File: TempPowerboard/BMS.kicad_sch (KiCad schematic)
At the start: 77 parts, among them IC1 BQ7694204PFBR, J1 Batt_Cells, J2 PEC02SAAN, Q1 NMOS, Q2 NMOS, Q3 NMOS, Q4 NMOS, Q5 FCX495TA

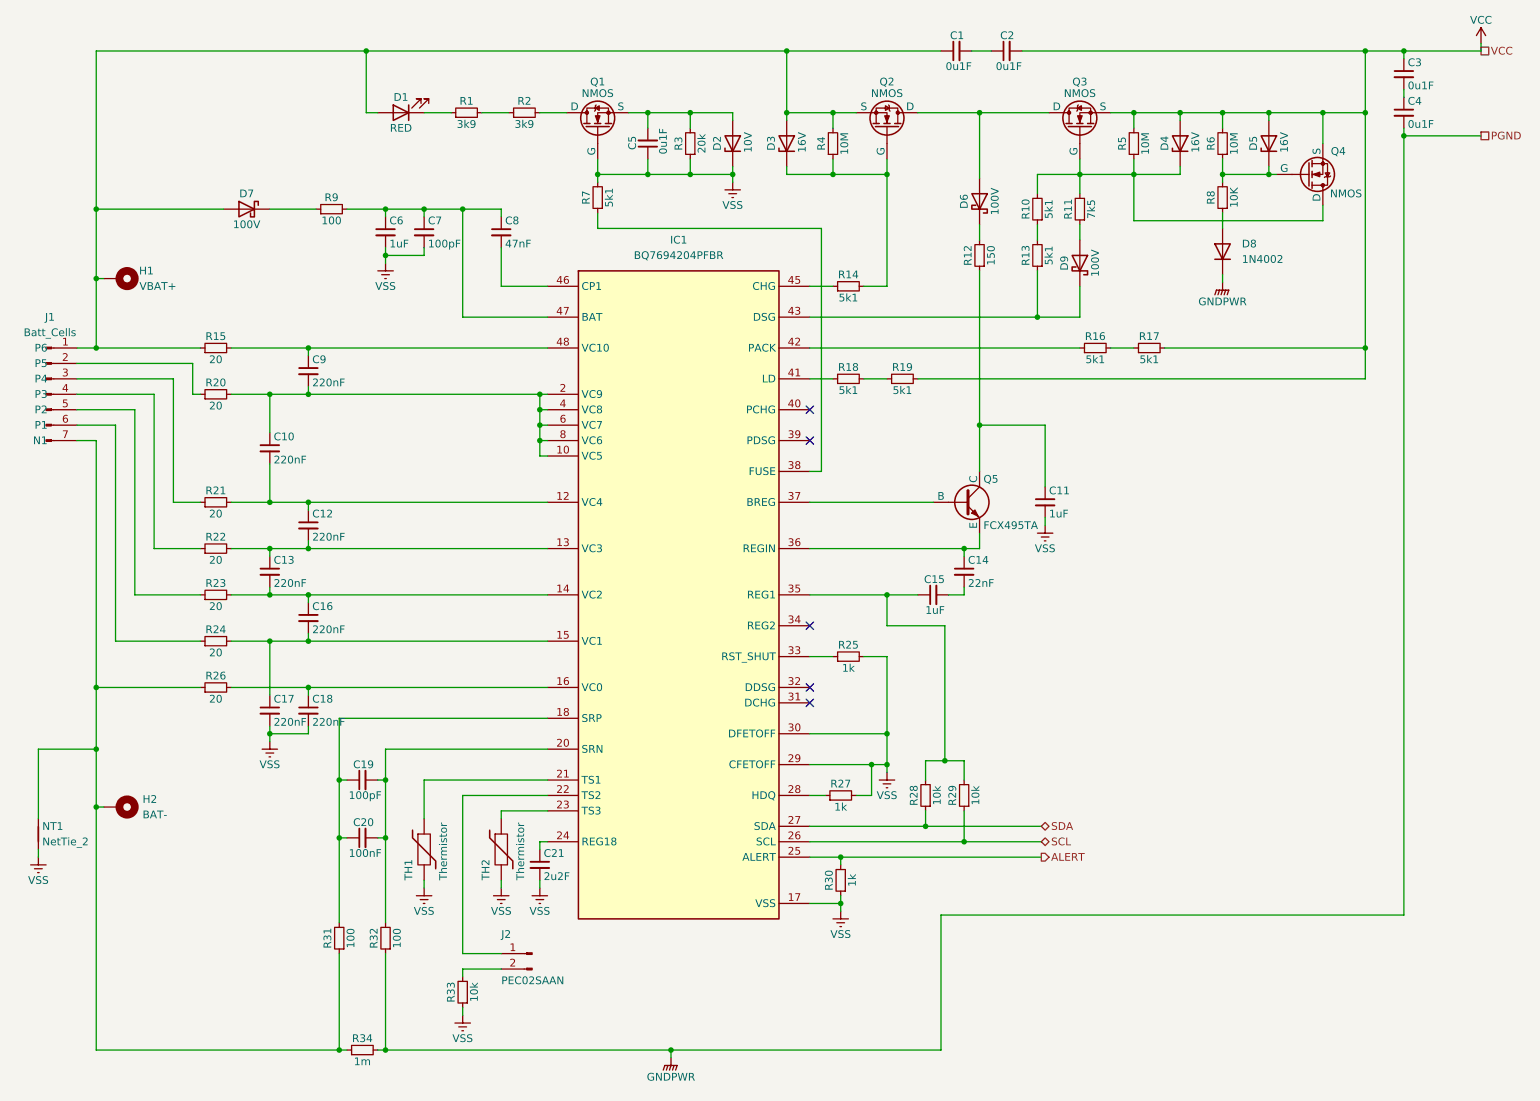
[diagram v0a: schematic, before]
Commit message: Devboard ports defined
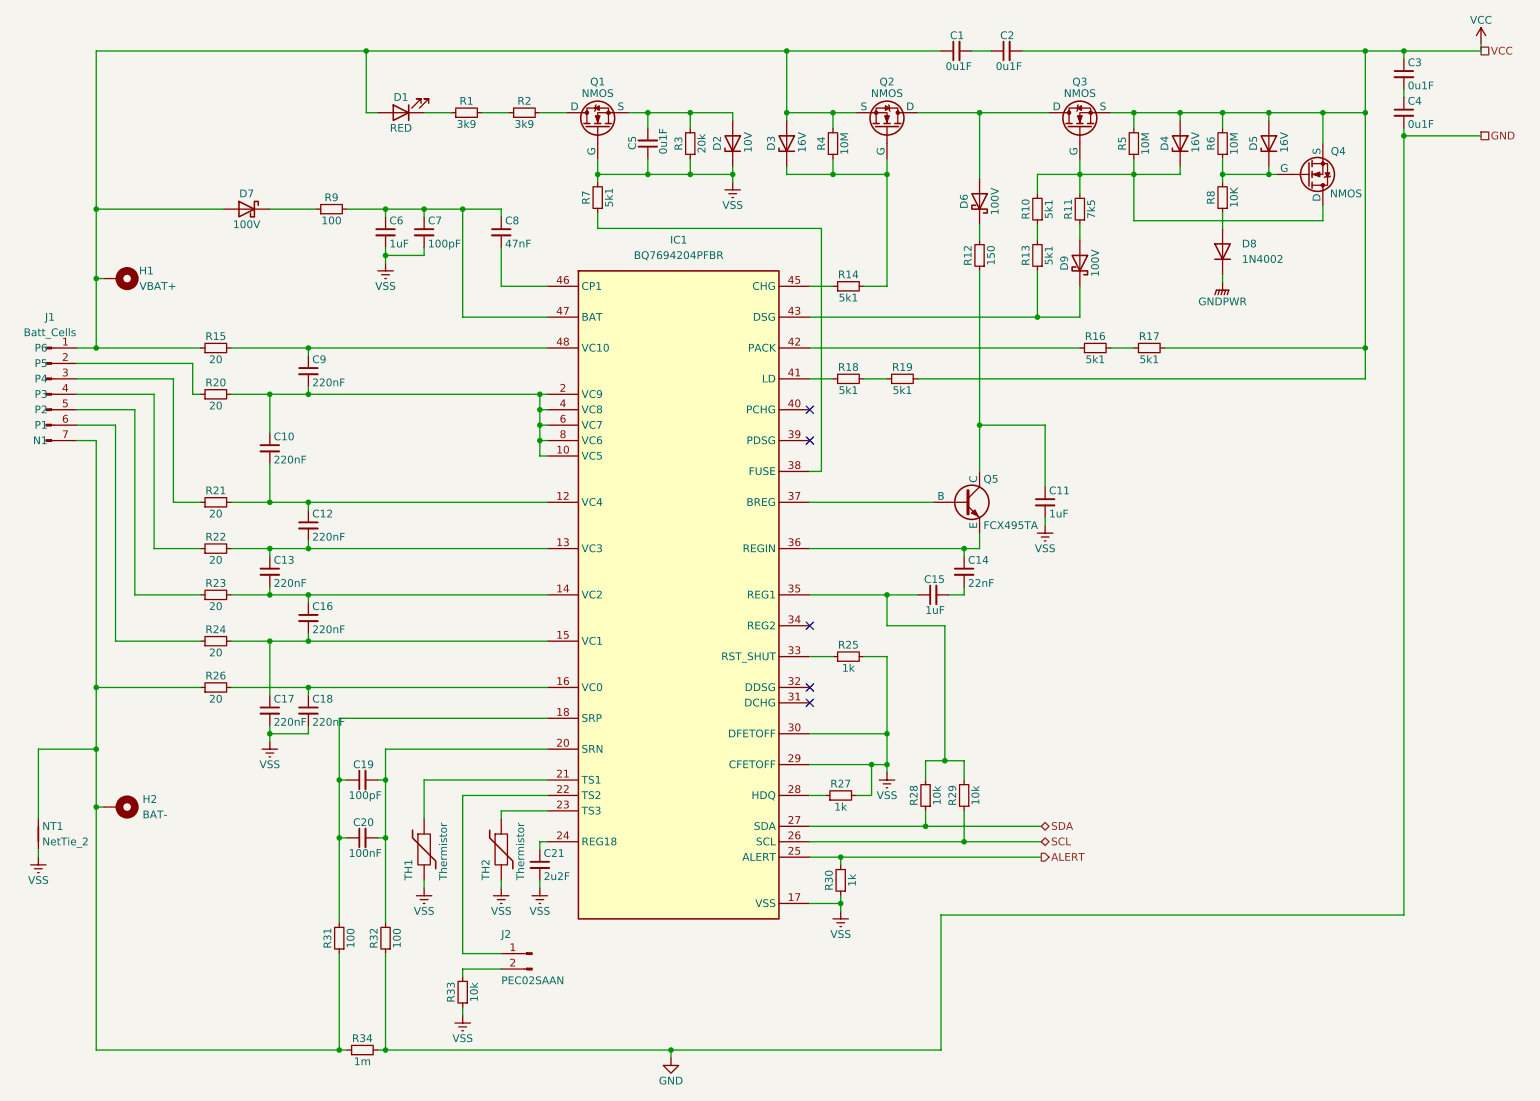
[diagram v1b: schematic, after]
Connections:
- net GNDPWR: no longer C4.2, R32.1, R34.2
- new net GND: C4.2, R32.1, R34.2
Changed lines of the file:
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@@
     (effects (font (size 1.27 1.27)) (justify left))
   )
-  (hierarchical_label "PGND" (shape passive) (at 260.35 33.655 0) (fields_autoplaced)
+  (hierarchical_label "GND" (shape passive) (at 260.35 33.655 0) (fields_autoplaced)
     (effects (font (size 1.27 1.27)) (justify left))
   )
@@
     )
   )
+  (symbol (lib_id "power:GND") (at 127 185.42 0) (unit 1)
+    (in_bom yes) (on_board yes) (dnp no)
+    (property "Reference" "#PWR023" (at 127 191.77 0)
+      (effects (font (size 1.27 1.27)) hide)
+    )
+    (property "Value" "GND" (at 127 189.23 0)
+      (effects (font (size 1.27 1.27)))
+    )
+    (property "Footprint" "" (at 127 185.42 0)
+      (effects (font (size 1.27 1.27)) hide)
+    )
+    (property "Datasheet" "" (at 127 185.42 0)
+      (effects (font (size 1.27 1.27)) hide)
+    )
+    (pin "1")
+    (instances
+      (project "TempPowerboard"
+        (path "/99c105bb-32a2-4c72-8069-227e584b9994/1eab3a2e-b7d4-4587-9e17-7f816eae63ec"
+          (reference "#PWR023") (unit 1)
+        )
+      )
+    )
+  )
   (symbol (lib_id "power:Earth") (at 137.16 41.275 0) (unit 1)
     (in_bom yes) (on_board yes) (dnp no)
@@
         )
       )
-    )
-  )
-  (symbol (lib_id "power:GNDPWR") (at 127 185.42 0) (unit 1)
-    (in_bom yes) (on_board yes) (dnp no)
-    (property "Reference" "#PWR038" (at 127 190.5 0)
-      (effects (font (size 1.27 1.27)) hide)
-    )
-    (property "Value" "GNDPWR" (at 127 188.595 0)
-      (effects (font (size 1.27 1.27)))
-    )
-    (property "Footprint" "" (at 127 186.69 0)
-      (effects (font (size 1.27 1.27)) hide)
-    )
-    (property "Datasheet" "" (at 127 186.69 0)
-      (effects (font (size 1.27 1.27)) hide)
-    )
-    (pin "1")
-    (instances
-      (project "TempPowerboard"
-        (path "/99c105bb-32a2-4c72-8069-227e584b9994/1eab3a2e-b7d4-4587-9e17-7f816eae63ec"
-          (reference "#PWR038") (unit 1)
-        )
-      )
